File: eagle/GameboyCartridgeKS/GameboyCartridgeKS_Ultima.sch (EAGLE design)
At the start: 23 parts, among them IC1 AT49F040J

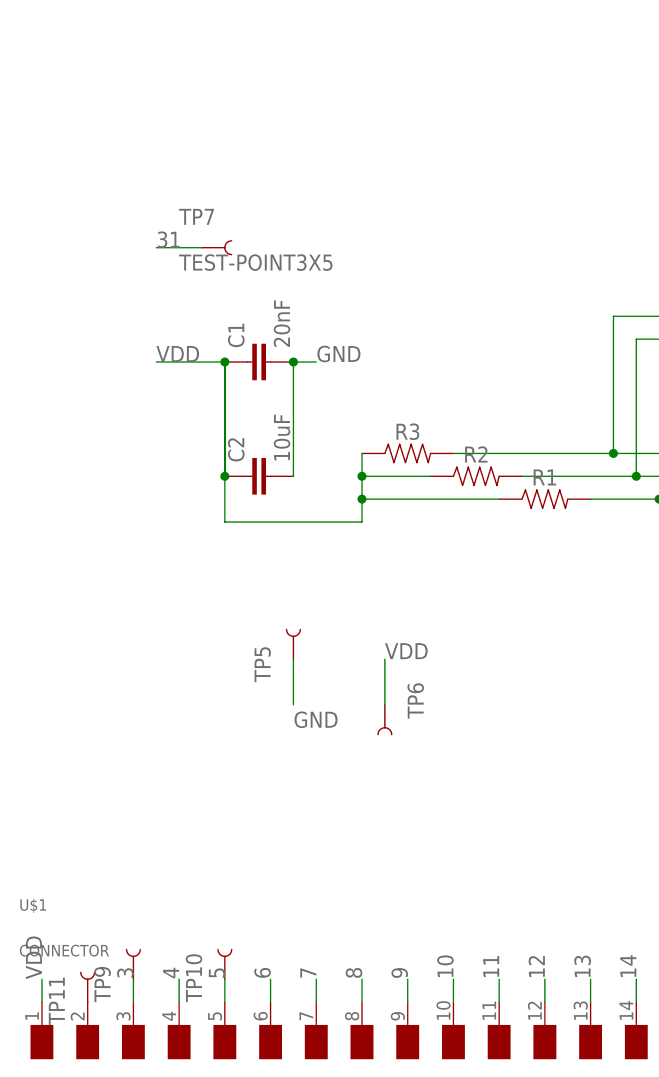
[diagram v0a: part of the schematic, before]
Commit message: Ultima GB cart looks fine and ready to prod. Will avoid to rush and post to the GB forum for feedback.
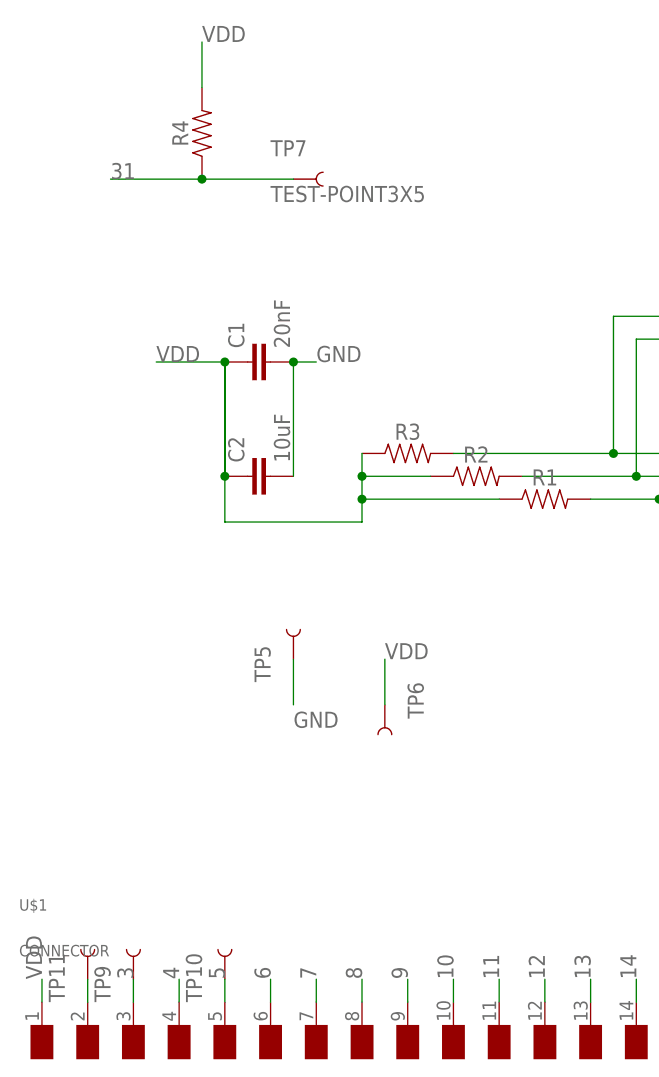
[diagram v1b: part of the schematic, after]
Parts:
- added R4: (no value), SparkFun-Resistors:RESISTOR1206
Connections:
- net 31: now also R4.1
- net VDD: now also R4.2
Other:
- moved on the sheet: TP11, TP7
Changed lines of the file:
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@@
 <part name="R3" library="SparkFun-Resistors" deviceset="RESISTOR" device="1206" value=" "/>
 <part name="TP13" library="SparkFun-Connectors" library_urn="urn:adsk.eagle:library:513" deviceset="TEST-POINT" device="3X5" package3d_urn="urn:adsk.eagle:package:38285/1"/>
+<part name="R4" library="SparkFun-Resistors" deviceset="RESISTOR" device="1206" value=" "/>
 </parts>
 <sheets>
@@
 <attribute name="NAME" x="33.02" y="88.9" size="1.778" layer="95" font="vector" rot="R270"/>
 </instance>
-<instance part="TP7" gate="G$1" x="10.16" y="137.16" smashed="yes">
-<attribute name="NAME" x="7.62" y="139.7" size="1.778" layer="95" font="vector"/>
-<attribute name="VALUE" x="7.62" y="134.62" size="1.778" layer="96" font="vector"/>
+<instance part="TP7" gate="G$1" x="20.32" y="144.78" smashed="yes">
+<attribute name="NAME" x="17.78" y="147.32" size="1.778" layer="95" font="vector"/>
+<attribute name="VALUE" x="17.78" y="142.24" size="1.778" layer="96" font="vector"/>
 </instance>
 <instance part="TP8" gate="G$1" x="139.7" y="55.88" smashed="yes" rot="R90">
@@
 <attribute name="NAME" x="10.16" y="53.34" size="1.778" layer="95" font="vector" rot="R90"/>
 </instance>
-<instance part="TP11" gate="G$1" x="-2.54" y="53.34" smashed="yes" rot="R90">
-<attribute name="NAME" x="-5.08" y="50.8" size="1.778" layer="95" font="vector" rot="R90"/>
+<instance part="TP11" gate="G$1" x="-2.54" y="55.88" smashed="yes" rot="R90">
+<attribute name="NAME" x="-5.08" y="53.34" size="1.778" layer="95" font="vector" rot="R90"/>
 </instance>
 <instance part="TP12" gate="G$1" x="91.44" y="119.38" smashed="yes" rot="R90">
@@
 <instance part="TP13" gate="G$1" x="106.68" y="86.36" smashed="yes" rot="R180">
 <attribute name="NAME" x="109.22" y="83.82" size="1.778" layer="95" font="vector" rot="R180"/>
+</instance>
+<instance part="R4" gate="G$1" x="10.16" y="149.86" smashed="yes" rot="R90">
+<attribute name="NAME" x="8.636" y="149.86" size="1.778" layer="95" font="vector" rot="R90" align="bottom-center"/>
+<attribute name="VALUE" x="9.144" y="149.86" size="1.778" layer="96" font="vector" rot="R90" align="top-center"/>
 </instance>
 </instances>
@@
 <label x="30.48" y="91.44" size="1.778" layer="95"/>
 </segment>
+<segment>
+<pinref part="R4" gate="G$1" pin="2"/>
+<wire x1="10.16" y1="154.94" x2="10.16" y2="160.02" width="0.1524" layer="91"/>
+<label x="10.16" y="160.02" size="1.778" layer="95"/>
+</segment>
 </net>
 <net name="6" class="0">
@@
 <net name="31" class="0">
 <segment>
-<wire x1="10.16" y1="137.16" x2="5.08" y2="137.16" width="0.1524" layer="91"/>
-<label x="5.08" y="137.16" size="1.778" layer="95"/>
+<wire x1="10.16" y1="144.78" x2="0" y2="144.78" width="0.1524" layer="91"/>
+<label x="0" y="144.78" size="1.778" layer="95"/>
 <pinref part="TP7" gate="G$1" pin="1"/>
+<pinref part="R4" gate="G$1" pin="1"/>
+<junction x="10.16" y="144.78"/>
+<wire x1="10.16" y1="144.78" x2="20.32" y2="144.78" width="0.1524" layer="91"/>
 </segment>
 <segment>
@@
 <pinref part="U$1" gate="G$1" pin="NC"/>
 <pinref part="TP11" gate="G$1" pin="1"/>
-</segment>
-</net>
+<wire x1="-2.54" y1="55.88" x2="-2.54" y2="53.34" width="0.1524" layer="91"/>
+</segment>
+</net>

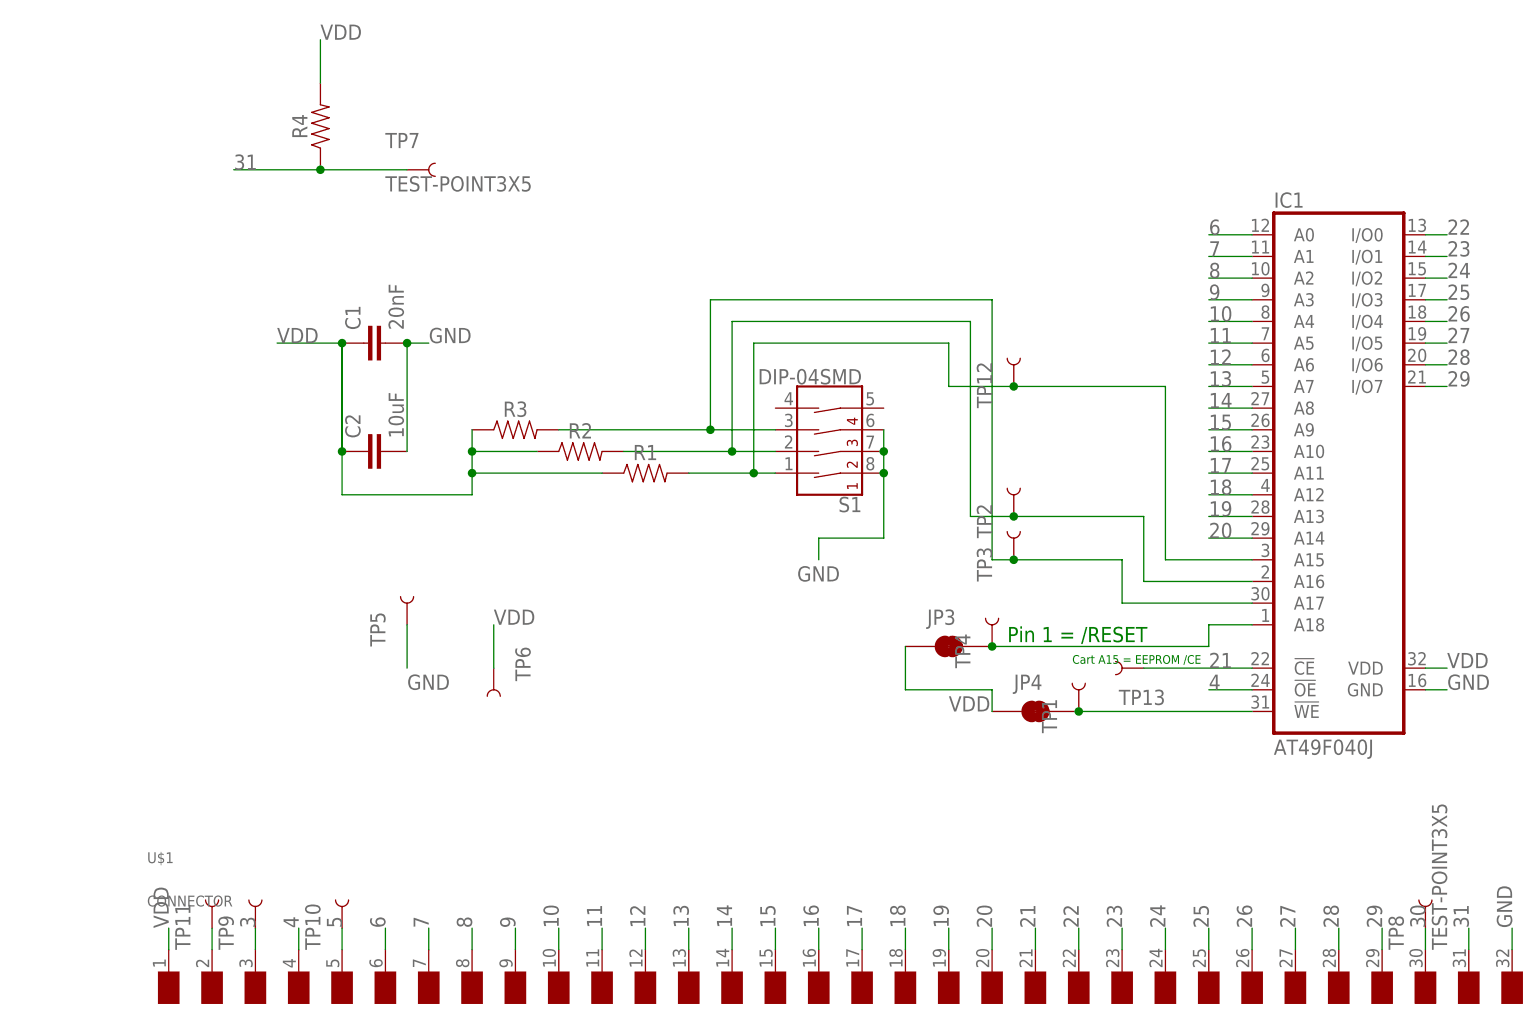
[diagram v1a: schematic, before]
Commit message: Added solderpads in addition to the SMD DIL toggle switch.
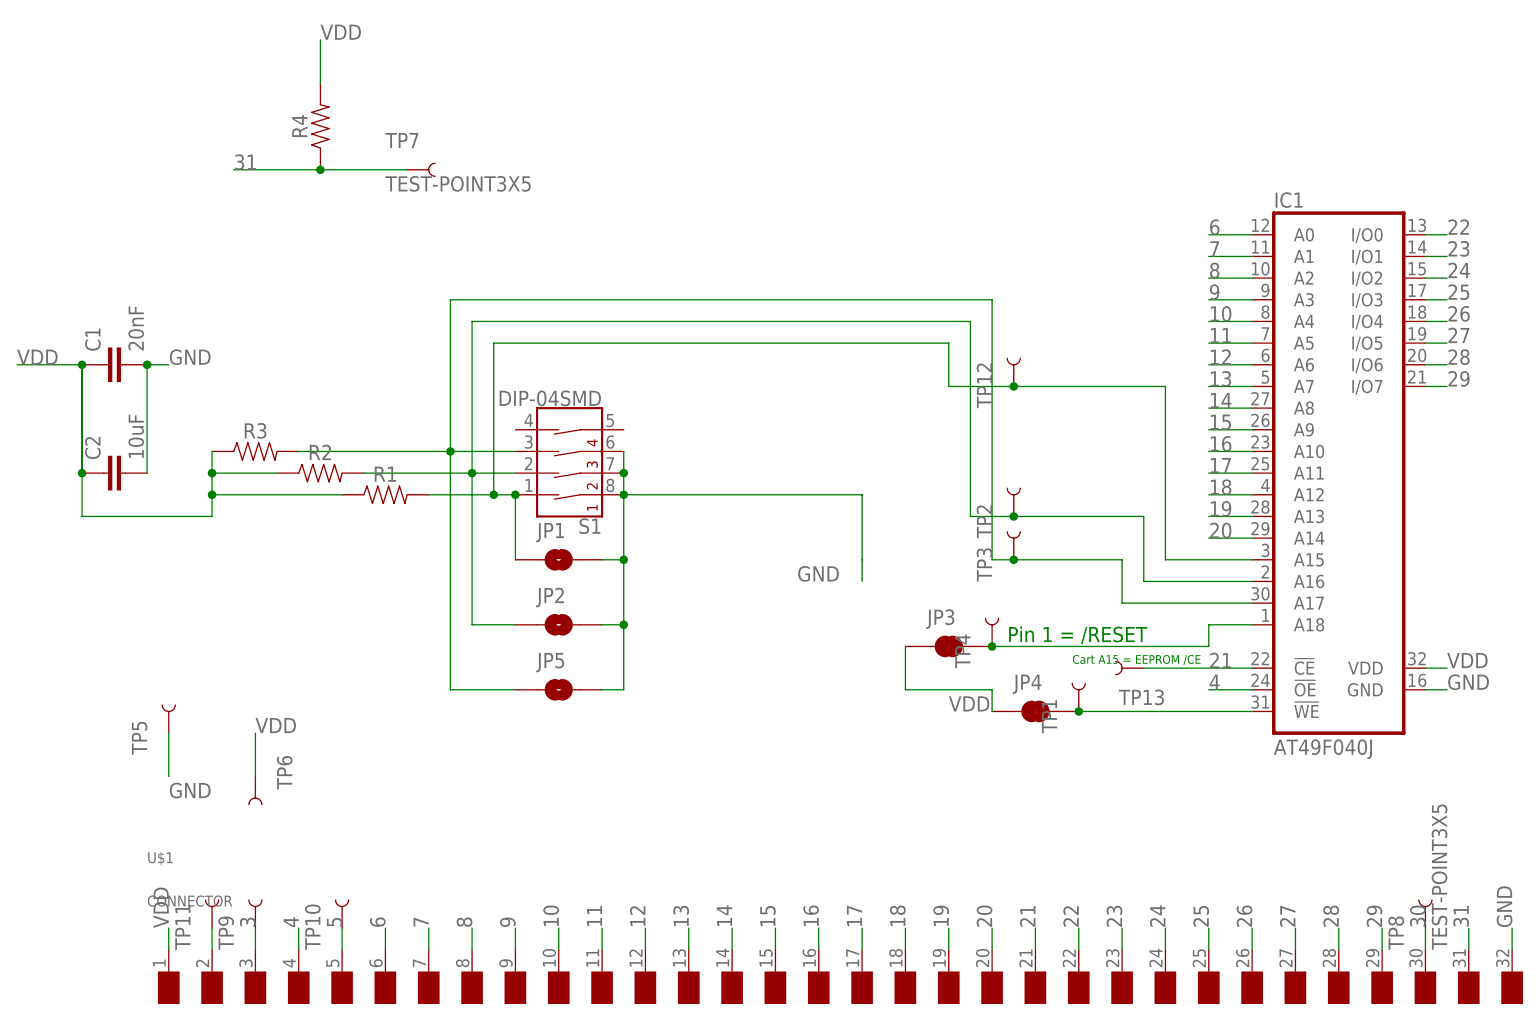
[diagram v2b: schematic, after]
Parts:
- added JP1, JP2, JP5: JUMPER-SMT_2_NO_NO-SILK, SparkFun-Jumpers:JUMPER-SMT_2_NO_NO-SILK
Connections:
- net GND: now also JP1.2, JP2.2, JP5.2
- net N$4: now also JP1.1
- net N$8: now also JP2.1
- net N$9: now also JP5.1
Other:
- moved on the sheet: C1, C2, R1, R2, R3, S1, TP5, TP6
